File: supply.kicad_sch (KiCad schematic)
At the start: 106 parts, among them J12 Molex_Nano-Fit_1x2_SMD_105430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, Q11 PJE138K, Q13 BCM857BS-7-F, Q14 BCM857BS-7-F, Q15 SSM3J332R, Q16 SSM3J332R, Q18 SSM3J332R, Q5 PJE138K, Q6 SSM3J332R, Q7 PJE138K, Q8 PJE138K, SW1 SW_SPDT_PCM12SMTR, U1 TPS56C230, U29 TPS56C230, U37 74LVC2G14_SOT457, U38 74LVC1G175_SOT457, U41 NCP730BMT330_WSON, U42 TPS7A0518P_SOT23-5

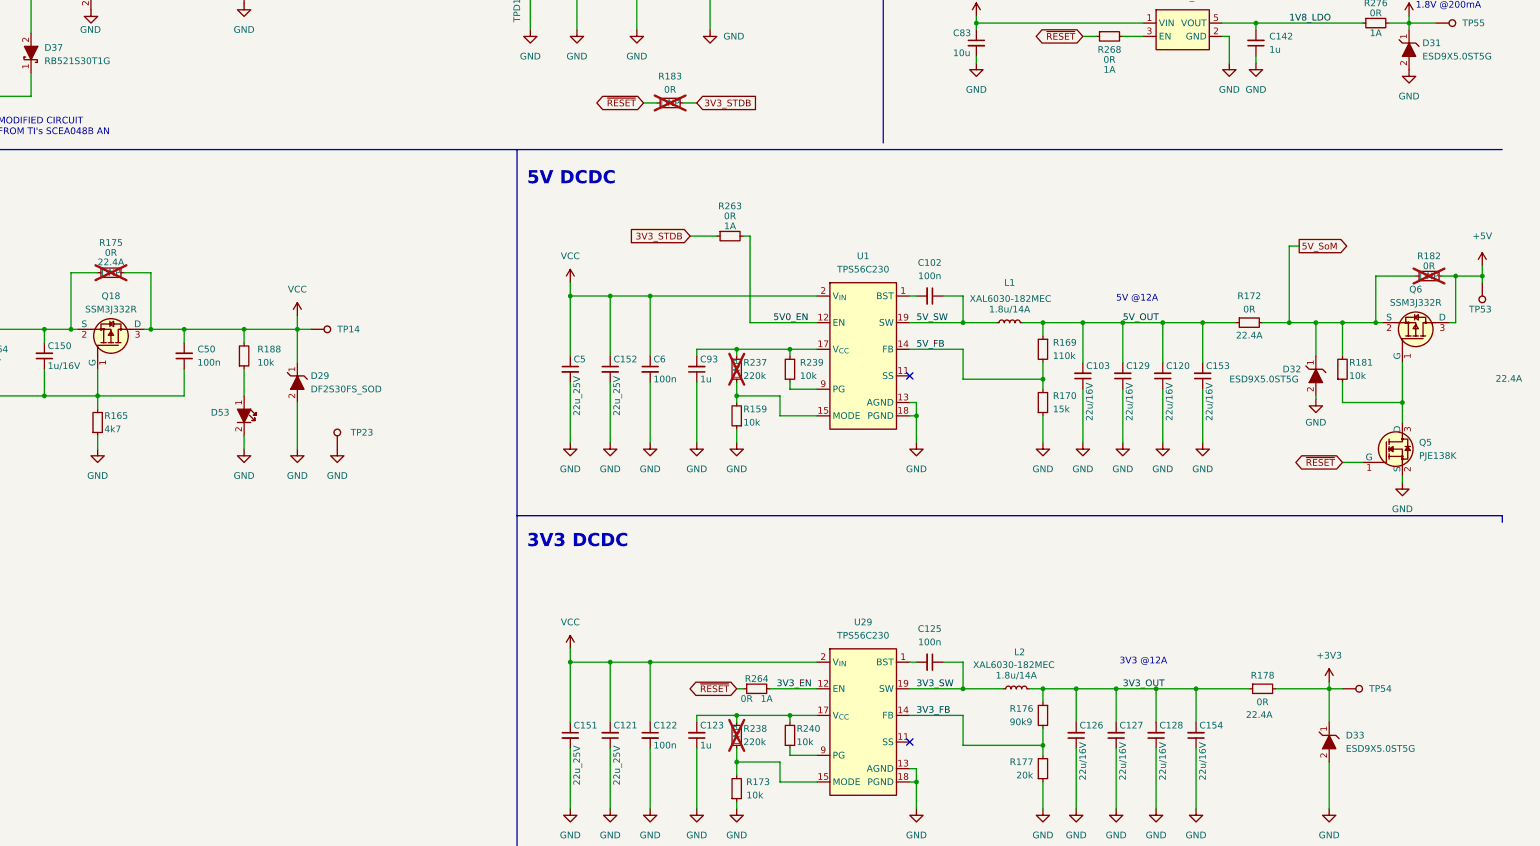
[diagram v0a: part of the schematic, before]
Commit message: 5/16 Commit: Sch Mods added and beginning Development on PCB layout
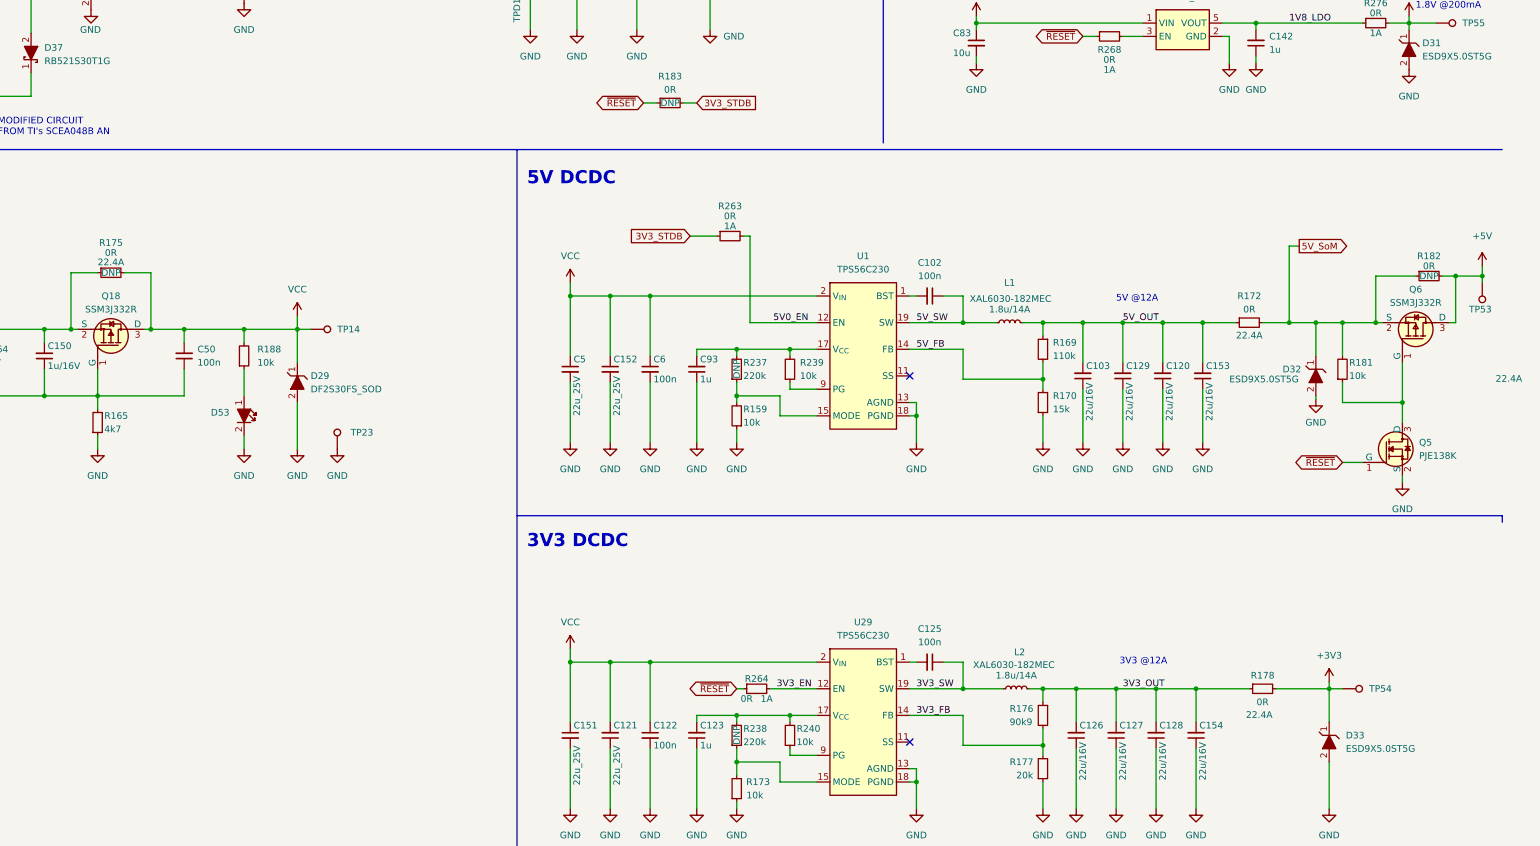
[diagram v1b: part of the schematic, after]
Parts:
- R175, R182, R183, R237, R238: now fitted
